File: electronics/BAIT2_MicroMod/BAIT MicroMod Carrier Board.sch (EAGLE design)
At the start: 156 parts, among them J1 SJ-43516-SMT, J10 QWIIC_RIGHT_ANGLE, J11 QWIIC_RIGHT_ANGLE, J15 BM05B-SRSS-TB(LF)(SN), J2 ST-TF-003A, J4 BM05B-SRSS-TB(LF)(SN), J5 QWIIC_RIGHT_ANGLE, J6 JST 2PH, J7 MICROMOD-2222-C, SW1 SKQGADE010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

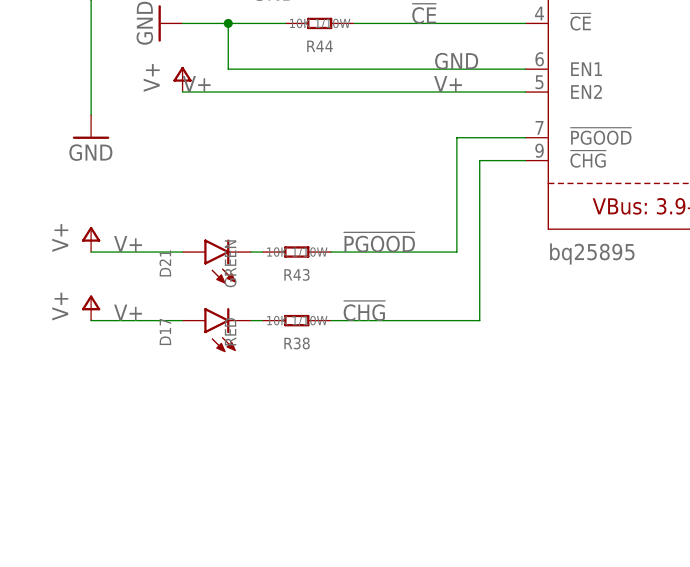
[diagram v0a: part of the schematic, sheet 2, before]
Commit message: Connected SD card detect pin to micromod
Resolves #25
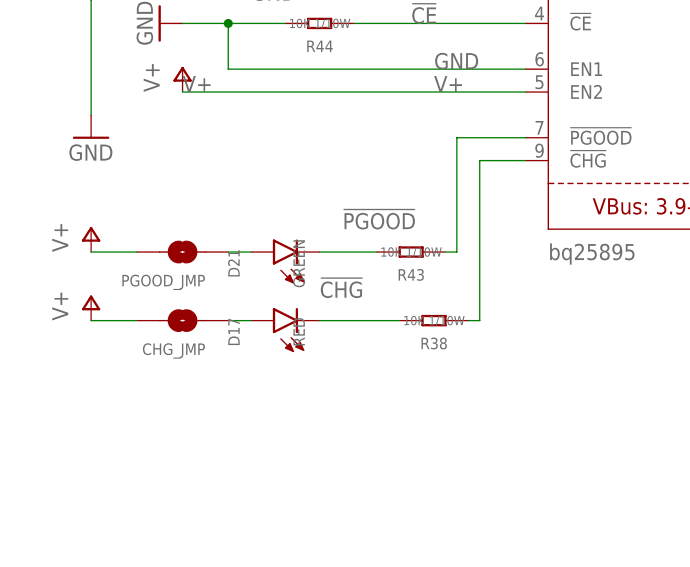
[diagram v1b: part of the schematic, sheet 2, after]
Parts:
- added CHG_JMP, PGOOD_JMP: JUMPER-SMT_2_NO_NO-SILK, SparkFun-Jumpers:JUMPER-SMT_2_NO_NO-SILK
- J_ASC, J_RSSI, J_RX, J_TX: value JUMPER-SMT_2_NC_TRACE_SILK -> JUMPER-SMT_2_NO_SILK; device SparkFun-Jumpers:JUMPER-SMT_2_NC_TRACE_SILK -> SparkFun-Jumpers:JUMPER-SMT_2_NO_SILK
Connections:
- new net N$75: D21.A, PGOOD_JMP.1
- new net N$76: CHG_JMP.1, D17.A
- new net SD_DETECT: J2.CD, J7.G5/BUS5
- net V+: now also CHG_JMP.2, PGOOD_JMP.2; no longer D17.A, D21.A
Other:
- moved on the sheet: D17, D21, R38, R43

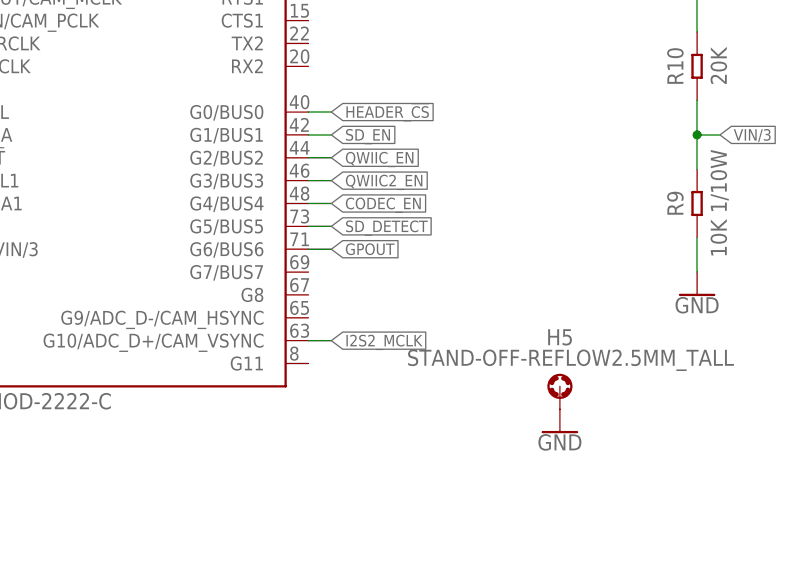
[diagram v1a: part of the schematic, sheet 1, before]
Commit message: Connect headphone switches to teensy ports
Resolves #24
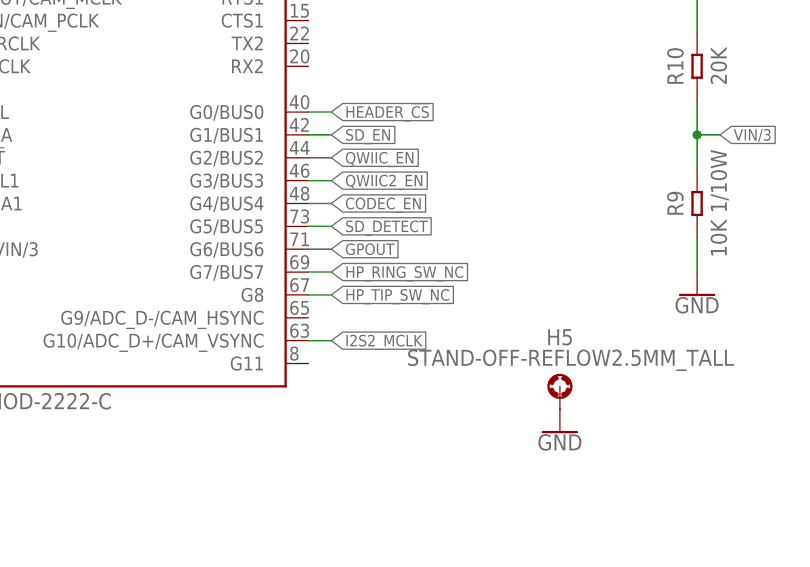
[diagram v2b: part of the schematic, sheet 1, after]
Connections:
- new net HP_RING_SW_NC: J1.RING_SWITCH, J7.G7/BUS7
- new net HP_TIP_SW_NC: J1.TIP_SWITCH, J7.G8
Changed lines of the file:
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@@
+</segment>
+</net>
+<net name="HP_RING_SW_NC" class="0">
+<segment>
+<pinref part="J7" gate="J1" pin="G7/BUS7"/>
+<wire x1="71.12" y1="149.86" x2="73.66" y2="149.86" width="0.1524" layer="91"/>
+<label x="73.66" y="149.86" size="1.27" layer="95" xref="yes"/>
+</segment>
+</net>
+<net name="HP_TIP_SW_NC" class="0">
+<segment>
+<pinref part="J7" gate="J1" pin="G8"/>
+<wire x1="71.12" y1="147.32" x2="73.66" y2="147.32" width="0.1524" layer="91"/>
+<label x="73.66" y="147.32" size="1.27" layer="95" xref="yes"/>
 </segment>
 </net>
@@
 </segment>
 </net>
+<net name="HP_RING_SW_NC" class="0">
+<segment>
+<pinref part="J1" gate="G$1" pin="RING_SWITCH"/>
+<wire x1="241.3" y1="203.2" x2="246.38" y2="203.2" width="0.1524" layer="91"/>
+<label x="246.38" y="203.2" size="1.27" layer="95" xref="yes"/>
+</segment>
+</net>
+<net name="HP_TIP_SW_NC" class="0">
+<segment>
+<pinref part="J1" gate="G$1" pin="TIP_SWITCH"/>
+<wire x1="241.3" y1="200.66" x2="246.38" y2="200.66" width="0.1524" layer="91"/>
+<label x="246.38" y="200.66" size="1.27" layer="95" xref="yes"/>
+</segment>
+</net>

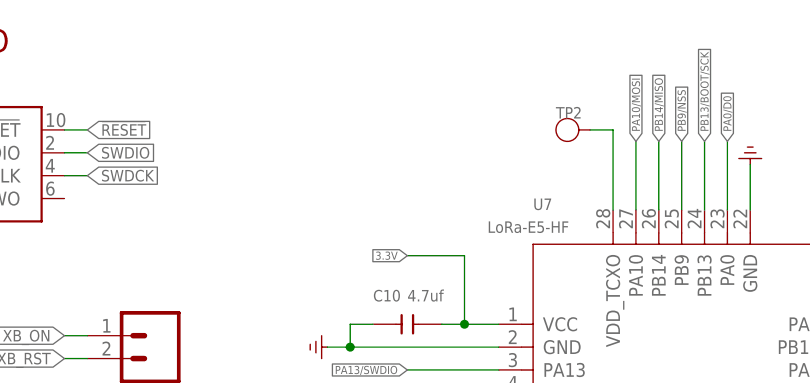
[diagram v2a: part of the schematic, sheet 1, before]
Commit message: Updates pin 24 connection on WIO
Solves #8
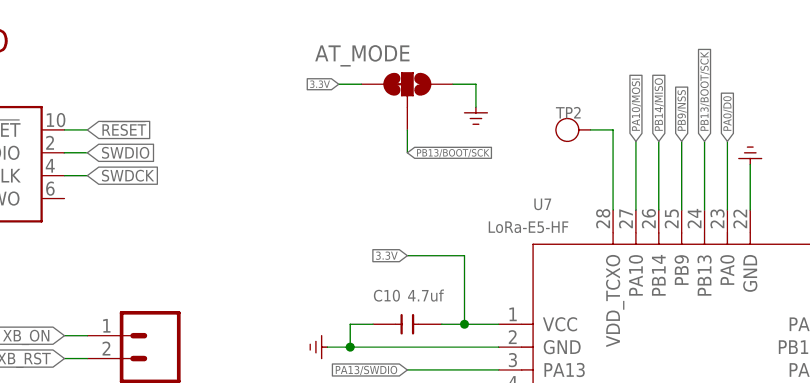
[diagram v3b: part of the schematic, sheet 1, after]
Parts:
- added AT_MODE: MK2_LR, SparkFun-Jumpers:JUMPER-SMT_3_1-NC_TRACE_SILK
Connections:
- net 3.3V: now also AT_MODE.3
- net GND: now also AT_MODE.1
- net PB13/BOOT/SCK: now also AT_MODE.2
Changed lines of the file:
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@@
 <part name="PGOOD_JMP" library="SparkFun-Jumpers" library_urn="urn:adsk.eagle:library:528" deviceset="JUMPER-SMT_2_NO" device="_NO-SILK" package3d_urn="urn:adsk.eagle:package:39277/1" value=""/>
 <part name="CHG_JMP" library="SparkFun-Jumpers" library_urn="urn:adsk.eagle:library:528" deviceset="JUMPER-SMT_2_NO" device="_NO-SILK" package3d_urn="urn:adsk.eagle:package:39277/1" value=""/>
+<part name="AT_MODE" library="SparkFun-Jumpers" library_urn="urn:adsk.eagle:library:528" deviceset="JUMPER-SMT_3_1-NC_TRACE" device="_SILK" package3d_urn="urn:adsk.eagle:package:39288/1" value="MK2_LR"/>
+<part name="G3" library="Power or GND " deviceset="GND_POWER" device=""/>
 </parts>
 <sheets>
@@
 0.410V drop at 1mA
 1.0V drop at 15mA</text>
-<attribute name="NAME" x="115.316" y="35.56" size="1.778" layer="95" font="vector" rot="R90" align="bottom-center"/>
-<attribute name="VALUE" x="118.364" y="35.56" size="1.778" layer="96" font="vector" rot="R90" align="top-center"/>
-<attribute name="VALUE" x="116.84" y="45.974" size="1.778" layer="96" align="bottom-center"/>
-<attribute name="NAME" x="127" y="35.814" size="1.778" layer="95" font="vector"/>
-<attribute name="VALUE" x="127" y="20.066" size="1.778" layer="96" font="vector" align="top-left"/>
-<attribute name="MPN" x="134.62" y="27.94" size="1.27" layer="96" display="off"/>
-<attribute name="VALUE" x="121.92" y="17.526" size="1.778" layer="96" align="top-center"/>
-<attribute name="NAME" x="150.241" y="21.336" size="1.778" layer="95" font="vector" rot="R270"/>
-<attribute name="VALUE" x="145.161" y="21.336" size="1.778" layer="96" font="vector" rot="R270"/>
-<attribute name="VALUE" x="147.32" y="14.986" size="1.778" layer="96" align="top-center"/>
-<attribute name="VALUE" x="119.38" y="40.64" size="1.778" layer="96" rot="R90"/>
 </plain>
 <instances>
@@
 <attribute name="VALUE" x="114.3" y="63.754" size="1.778" layer="96" align="bottom-center"/>
 </instance>
+<instance part="AT_MODE" gate="G$1" x="256.54" y="241.3" smashed="yes" rot="MR90">
+<attribute name="NAME" x="256.921" y="243.84" size="1.778" layer="95" font="vector" rot="MR0"/>
+</instance>
+<instance part="G3" gate="G$1" x="264.16" y="238.76" smashed="yes"/>
 </instances>
 <busses>
@@
 <pinref part="GND44" gate="1" pin="GND"/>
 </segment>
+<segment>
+<pinref part="AT_MODE" gate="G$1" pin="1"/>
+<wire x1="261.62" y1="241.3" x2="264.16" y2="241.3" width="0.1524" layer="91"/>
+<pinref part="G3" gate="G$1" pin="GND"/>
+<wire x1="264.16" y1="241.3" x2="264.16" y2="238.76" width="0.1524" layer="91"/>
+</segment>
 </net>
 <net name="3.3V" class="1">
@@
 <pinref part="SUPPLY8" gate="G$1" pin="3.3V"/>
 <wire x1="119.38" y1="60.96" x2="119.38" y2="63.5" width="0.1524" layer="91"/>
+</segment>
+<segment>
+<pinref part="AT_MODE" gate="G$1" pin="3"/>
+<wire x1="251.46" y1="241.3" x2="248.92" y2="241.3" width="0.1524" layer="91"/>
+<label x="248.92" y="241.3" size="0.8128" layer="95" rot="R180" xref="yes"/>
 </segment>
 </net>
@@
 <pinref part="E5_EXTRA_PINS" gate="G$1" pin="2"/>
 </segment>
+<segment>
+<pinref part="AT_MODE" gate="G$1" pin="2"/>
+<wire x1="256.54" y1="236.22" x2="256.54" y2="233.68" width="0.1524" layer="91"/>
+<label x="256.54" y="233.68" size="0.8128" layer="95" xref="yes"/>
+</segment>
 </net>
 <net name="PA14/SWCLK" class="0">
@@
 <pinref part="U3" gate="G$1" pin="OUT"/>
 <pinref part="C13" gate="G$1" pin="1"/>
-<wire x1="43.18" y1="55.88" x2="48.26" y2="55.88" width="0.1524" layer="91" grouprefs="REGS_3V QWIIC"/>
+<wire x1="43.18" y1="55.88" x2="48.26" y2="55.88" width="0.1524" layer="91" grouprefs="QWIIC REGS_3V"/>
 <wire x1="48.26" y1="54.61" x2="48.26" y2="55.88" width="0.1524" layer="91" grouprefs="REGS_3V"/>
 <junction x="48.26" y="55.88" grouprefs="REGS_3V"/>

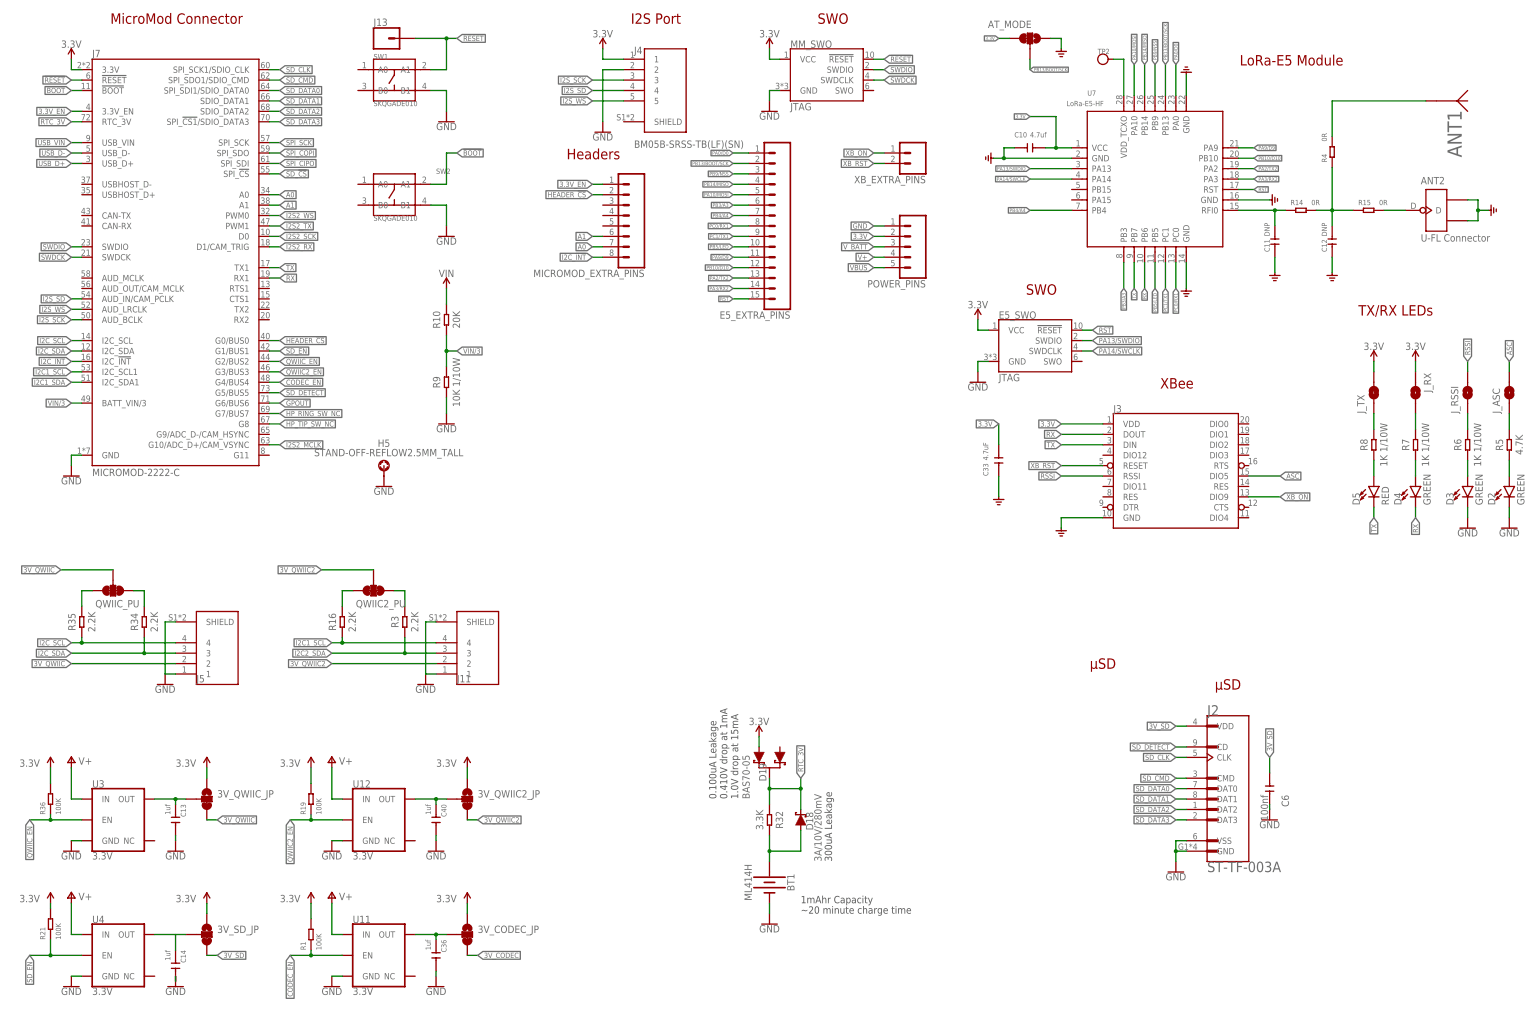
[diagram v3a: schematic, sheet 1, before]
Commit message: Updated layout for TC2956 chip
Should resolve #29, but I should double check
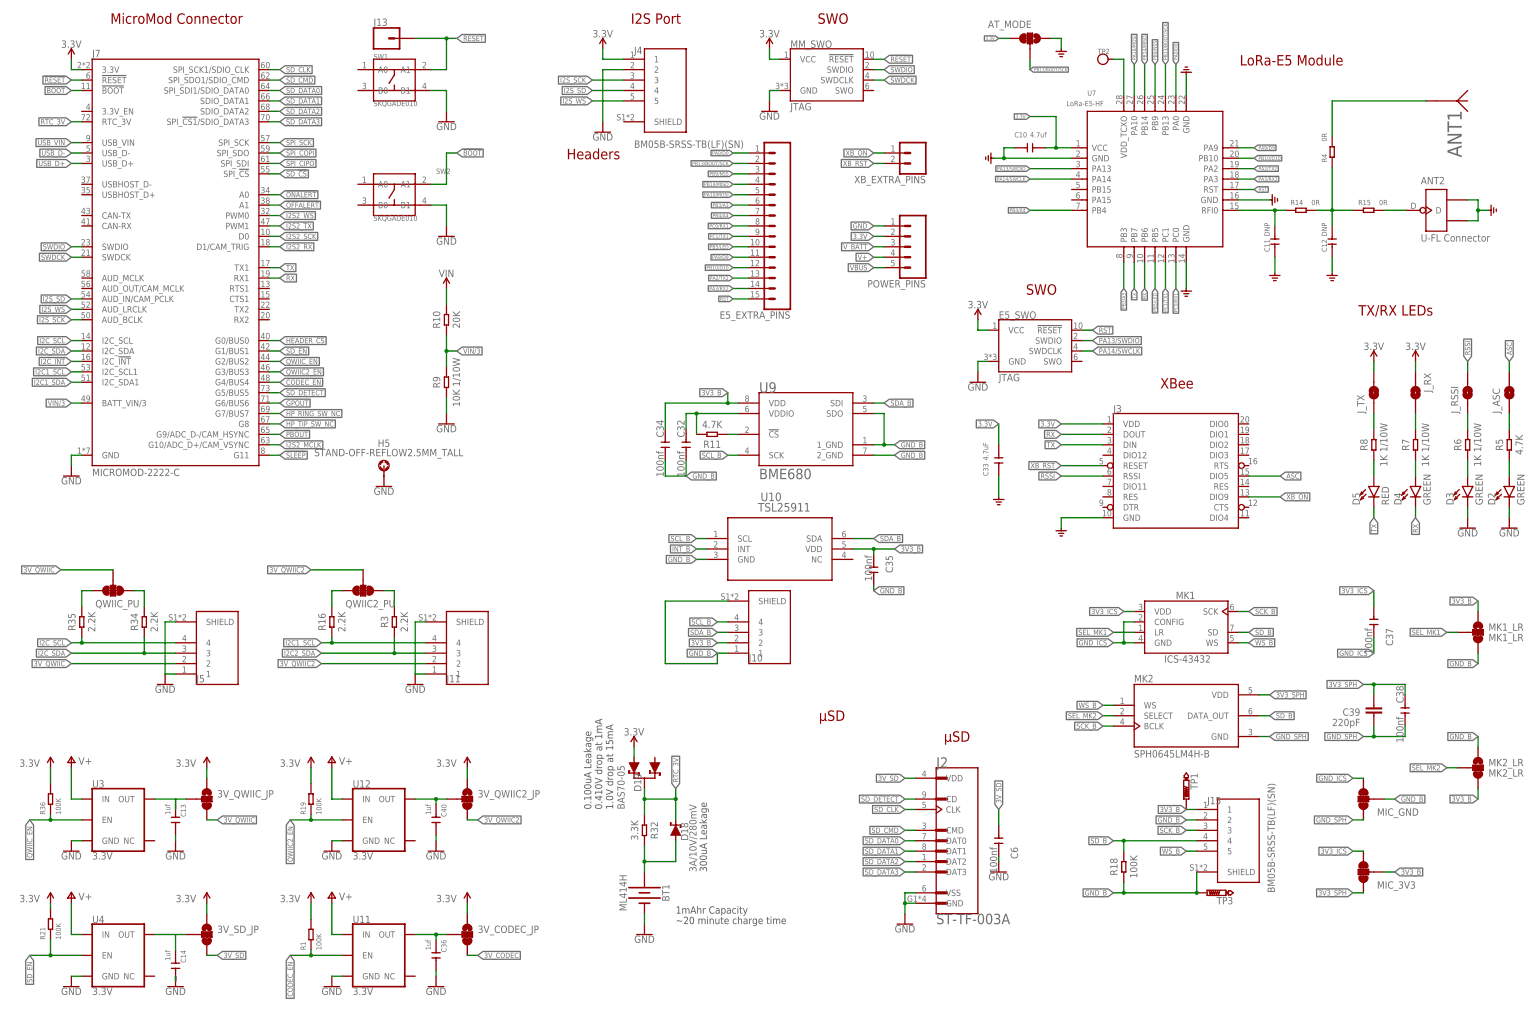
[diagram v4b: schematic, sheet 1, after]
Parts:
- removed MICROMOD_EXTRA_PINS: (no value), SparkFun-Connectors:CONN_08"
- added BATT_PWR, USB_PWR: JUMPER-SMT_2_NO_NO-SILK, SparkFun-Jumpers:JUMPER-SMT_2_NO_NO-SILK
- added C41: 100nf, OPL_Capacitor:CERAMIC-100NF-50V-10%-X7R(0603)
- added J12: L203011MS02QECONN8_MS02QE_CNK, BAIT-Components:L203011MS02QECONN8_MS02QE_CNK
- added JP2, JP3, JP4: JUMPER-SMT_2_NC_TRACE_NO-SILK, SparkFun-Jumpers:JUMPER-SMT_2_NC_TRACE_NO-SILK
- added R20: 100K, OPL_Resistor:SMD-RES-100K-1%-1/10W(0603)
- added R22: 1.02M, OPL_Resistor:SMD-RES-100K-1%-1/10W(0603)
- added R25: 61.9k, OPL_Resistor:SMD-RES-100K-1%-1/10W(0603)
- added R26: 115k, OPL_Resistor:SMD-RES-100K-1%-1/10W(0603)
- added R27, R28, R29: (no value), SparkFun-Resistors:RESISTORAXIAL-0.3
- added SW3: SKQGADE010, OPL_Switch:SMD-BUTTON(4P-5.2X5.2X1.5MM-SKQGADE010)-SKQGADE010
- added U13: LTC2956IMS-1PBF, BAIT-Components:LTC2956IMS-1PBF
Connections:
- removed net 3.3V_EN: J7.3.3V_EN, MICROMOD_EXTRA_PINS.1
- removed net A0: J7.A0, MICROMOD_EXTRA_PINS.7
- removed net A1: J7.A1, MICROMOD_EXTRA_PINS.6
- new net !OFFALERT!: J7.A1, U13.!OFFALERT
- new net !ONALERT!: J7.A0, U13.!ONALERT
- new net !PB: SW3.A1, U13.!PB
- new net !PBOUT!: J7.G9/ADC_D-/CAM_HSYNC, U13.!PBOUT
- new net !SLEEP!: J7.G11, U13.!SLEEP
- new net 3V_EN: U13.EN/!EN, U8.ON/OFF
- new net N$77: U3.OUT
- new net N$78: JP3.2, R20.2, R28.2, U13.RANGE
- new net N$79: JP2.1, R22.2
- new net N$80: JP4.2, R29.2, U13.PERIOD
- new net N$81: JP2.2, R20.1, R27.2, U13.LONG
- new net N$82: JP3.1, R25.2
- new net N$83: JP4.1, R26.2
- new net V_BATT_IN: BATT_PWR.2, J12.6, J6.2
- new net V_USB_IN: D15.C, J12.2, USB_PWR.2
- net 3V_QWIIC_OUT: no longer U3.OUT
- net GND: now also C41.2, R22.1, R25.1, R26.1, R27.1, R28.1, R29.1, SW3.B1, U13.GND, U13.ONMAX
- net HEADER_!CS!: no longer MICROMOD_EXTRA_PINS.2
- net I2C_!INT!: no longer MICROMOD_EXTRA_PINS.8
- net V+: now also C41.1, U13.VIN; no longer U8.ON/OFF
- net VBUS: now also J12.1, J12.3, USB_PWR.1; no longer D15.C
- net VIN: now also BATT_PWR.1, J12.5, J12.7; no longer J6.2
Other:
- note added: "External capacitor (optional) jumpers"
- note added: "ONMAX is tied to GND because the watchdog is not used. R_LONG is 1.02 MOhms > Power up RUN and 8.2s LONG press delay. R_RANGE is 61.9 kOhms > period between 102s and 14m R_PERIOD is 117 kOhms > a 5 minute sleep cycle (1024 * 117) / 400 = 299.5s *115k would give 5 seconds of uptime before 5 minutes passed), but I should account for the resistor error."
- moved on the sheet: BT1, C6, D18, D19, J11, J2, QWIIC2_PU, R16, R3, R32
